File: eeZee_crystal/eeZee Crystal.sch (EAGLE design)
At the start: 4 parts, among them Q1 16MHz

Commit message: Changed 3-pin header to vertical style (displays better in Eagle)
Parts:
- JP1: device pinhead-2:PINHD-1X03_2.54-90°-S -> pinhead-2:PINHD-1X03_2.54-S
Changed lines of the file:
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@@
 <?xml version="1.0" encoding="utf-8"?>
 <!DOCTYPE eagle SYSTEM "eagle.dtd">
-<eagle version="6.0">
+<eagle version="6.1">
 <drawing>
 <settings>
@@
 <layer number="49" name="Reference" color="7" fill="1" visible="yes" active="no"/>
 <layer number="50" name="dxf" color="7" fill="1" visible="yes" active="no"/>
-<layer number="51" name="tDocu" color="7" fill="1" visible="yes" active="no"/>
+<layer number="51" name="tDocu" color="11" fill="1" visible="yes" active="no"/>
 <layer number="52" name="bDocu" color="7" fill="1" visible="yes" active="no"/>
 <layer number="53" name="tPadExt" color="7" fill="1" visible="yes" active="no"/>
@@
 <attribute name="PARTNO" value="C1608C0G1H080D"/>
 </part>
-<part name="JP1" library="pinhead-2" deviceset="PINHD-1X03" device="_2.54-90°-S" value="XTAL">
+<part name="JP1" library="pinhead-2" deviceset="PINHD-1X03" device="_2.54-S" value="XTAL">
 <attribute name="BOM" value="EXCLUDE"/>
 </part>

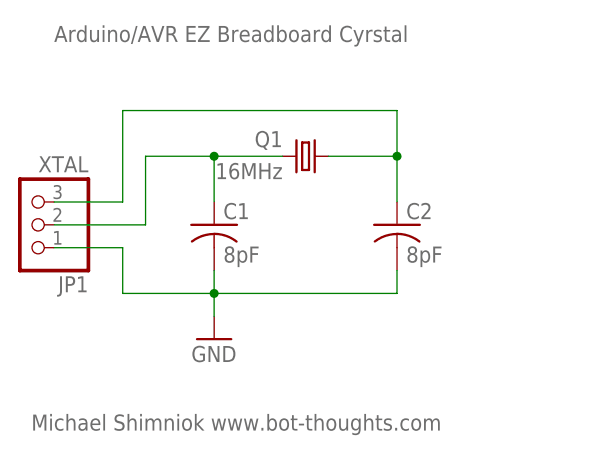
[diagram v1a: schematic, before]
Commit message: Resized board narrower and aligned to inches. Added silk for multiple frequencies. Mitred corners. Changed silk print sizes.
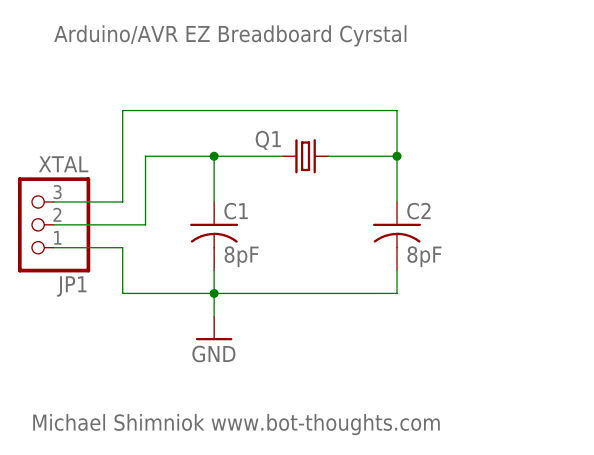
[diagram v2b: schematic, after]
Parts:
- Q1: value 16MHz -> (none)
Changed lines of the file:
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@@
 <?xml version="1.0" encoding="utf-8"?>
 <!DOCTYPE eagle SYSTEM "eagle.dtd">
-<eagle version="6.1">
+<eagle version="6.4">
 <drawing>
 <settings>
@@
 <grid distance="0.1" unitdist="inch" unit="inch" style="lines" multiple="1" display="no" altdistance="0.01" altunitdist="inch" altunit="inch"/>
 <layers>
-<layer number="1" name="Top" color="4" fill="1" visible="yes" active="no"/>
-<layer number="16" name="Bottom" color="1" fill="1" visible="yes" active="no"/>
-<layer number="17" name="Pads" color="2" fill="1" visible="yes" active="no"/>
-<layer number="18" name="Vias" color="2" fill="1" visible="yes" active="no"/>
-<layer number="19" name="Unrouted" color="6" fill="1" visible="yes" active="no"/>
-<layer number="20" name="Dimension" color="15" fill="1" visible="yes" active="no"/>
-<layer number="21" name="tPlace" color="7" fill="1" visible="yes" active="no"/>
-<layer number="22" name="bPlace" color="7" fill="1" visible="yes" active="no"/>
-<layer number="23" name="tOrigins" color="15" fill="1" visible="yes" active="no"/>
-<layer number="24" name="bOrigins" color="15" fill="1" visible="yes" active="no"/>
-<layer number="25" name="tNames" color="7" fill="1" visible="yes" active="no"/>
-<layer number="26" name="bNames" color="7" fill="1" visible="yes" active="no"/>
-<layer number="27" name="tValues" color="7" fill="1" visible="yes" active="no"/>
-<layer number="28" name="bValues" color="7" fill="1" visible="yes" active="no"/>
+<layer number="1" name="Top" color="4" fill="1" visible="no" active="no"/>
+<layer number="16" name="Bottom" color="1" fill="1" visible="no" active="no"/>
+<layer number="17" name="Pads" color="2" fill="1" visible="no" active="no"/>
+<layer number="18" name="Vias" color="2" fill="1" visible="no" active="no"/>
+<layer number="19" name="Unrouted" color="6" fill="1" visible="no" active="no"/>
+<layer number="20" name="Dimension" color="15" fill="1" visible="no" active="no"/>
+<layer number="21" name="tPlace" color="7" fill="1" visible="no" active="no"/>
+<layer number="22" name="bPlace" color="7" fill="1" visible="no" active="no"/>
+<layer number="23" name="tOrigins" color="15" fill="1" visible="no" active="no"/>
+<layer number="24" name="bOrigins" color="15" fill="1" visible="no" active="no"/>
+<layer number="25" name="tNames" color="7" fill="1" visible="no" active="no"/>
+<layer number="26" name="bNames" color="7" fill="1" visible="no" active="no"/>
+<layer number="27" name="tValues" color="7" fill="1" visible="no" active="no"/>
+<layer number="28" name="bValues" color="7" fill="1" visible="no" active="no"/>
 <layer number="29" name="tStop" color="7" fill="3" visible="no" active="no"/>
 <layer number="30" name="bStop" color="7" fill="6" visible="no" active="no"/>
@@
 <layer number="35" name="tGlue" color="7" fill="4" visible="no" active="no"/>
 <layer number="36" name="bGlue" color="7" fill="5" visible="no" active="no"/>
-<layer number="37" name="tTest" color="7" fill="1" visible="yes" active="no"/>
-<layer number="38" name="bTest" color="7" fill="1" visible="yes" active="no"/>
+<layer number="37" name="tTest" color="7" fill="1" visible="no" active="no"/>
+<layer number="38" name="bTest" color="7" fill="1" visible="no" active="no"/>
 <layer number="39" name="tKeepout" color="4" fill="11" visible="no" active="no"/>
 <layer number="40" name="bKeepout" color="1" fill="11" visible="no" active="no"/>
@@
 <layer number="44" name="Drills" color="7" fill="1" visible="no" active="no"/>
 <layer number="45" name="Holes" color="7" fill="1" visible="no" active="no"/>
-<layer number="46" name="Milling" color="3" fill="1" visible="yes" active="no"/>
-<layer number="47" name="Measures" color="7" fill="1" visible="yes" active="no"/>
-<layer number="48" name="Document" color="7" fill="1" visible="yes" active="no"/>
-<layer number="49" name="Reference" color="7" fill="1" visible="yes" active="no"/>
-<layer number="50" name="dxf" color="7" fill="1" visible="yes" active="no"/>
-<layer number="51" name="tDocu" color="11" fill="1" visible="yes" active="no"/>
-<layer number="52" name="bDocu" color="7" fill="1" visible="yes" active="no"/>
-<layer number="53" name="tPadExt" color="7" fill="1" visible="yes" active="no"/>
-<layer number="54" name="bPadExt" color="1" fill="1" visible="yes" active="no"/>
-<layer number="56" name="wert" color="7" fill="1" visible="yes" active="no"/>
+<layer number="46" name="Milling" color="3" fill="1" visible="no" active="no"/>
+<layer number="47" name="Measures" color="7" fill="1" visible="no" active="no"/>
+<layer number="48" name="Document" color="7" fill="1" visible="no" active="no"/>
+<layer number="49" name="Reference" color="7" fill="1" visible="no" active="no"/>
+<layer number="50" name="dxf" color="7" fill="1" visible="no" active="no"/>
+<layer number="51" name="tDocu" color="11" fill="1" visible="no" active="no"/>
+<layer number="52" name="bDocu" color="7" fill="1" visible="no" active="no"/>
+<layer number="53" name="tPadExt" color="7" fill="1" visible="no" active="no"/>
+<layer number="54" name="bPadExt" color="1" fill="1" visible="no" active="no"/>
+<layer number="56" name="wert" color="7" fill="1" visible="no" active="no"/>
 <layer number="91" name="Nets" color="2" fill="1" visible="yes" active="yes"/>
 <layer number="92" name="Busses" color="1" fill="1" visible="yes" active="yes"/>
@@
 </classes>
 <parts>
-<part name="Q1" library="mes_crystal" deviceset="CRYSTAL" device="NDK5X3" value="16MHz">
+<part name="Q1" library="mes_crystal" deviceset="CRYSTAL" device="NDK5X3">
 <attribute name="PARTNO" value="NX5032GA-16.000000MHZ-LN-CD-1"/>
 </part>

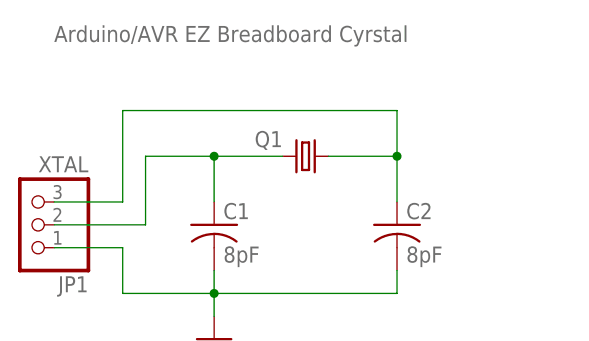
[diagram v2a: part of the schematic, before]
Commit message: Increaed spacing to 8/10mil for most objects, reduced distance to 10mil.
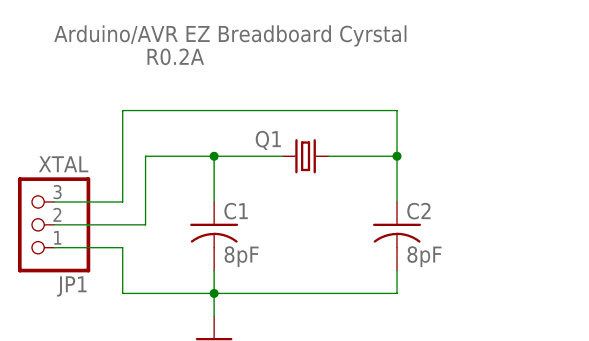
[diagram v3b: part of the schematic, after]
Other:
- note added: "R0.2A"
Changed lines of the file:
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@@
 <text x="25.4" y="48.26" size="1.778" layer="95">Arduino/AVR EZ Breadboard Cyrstal</text>
 <text x="22.86" y="5.08" size="1.778" layer="95">Michael Shimniok www.bot-thoughts.com</text>
+<text x="35.56" y="45.72" size="1.778" layer="95">R0.2A</text>
 </plain>
 <instances>

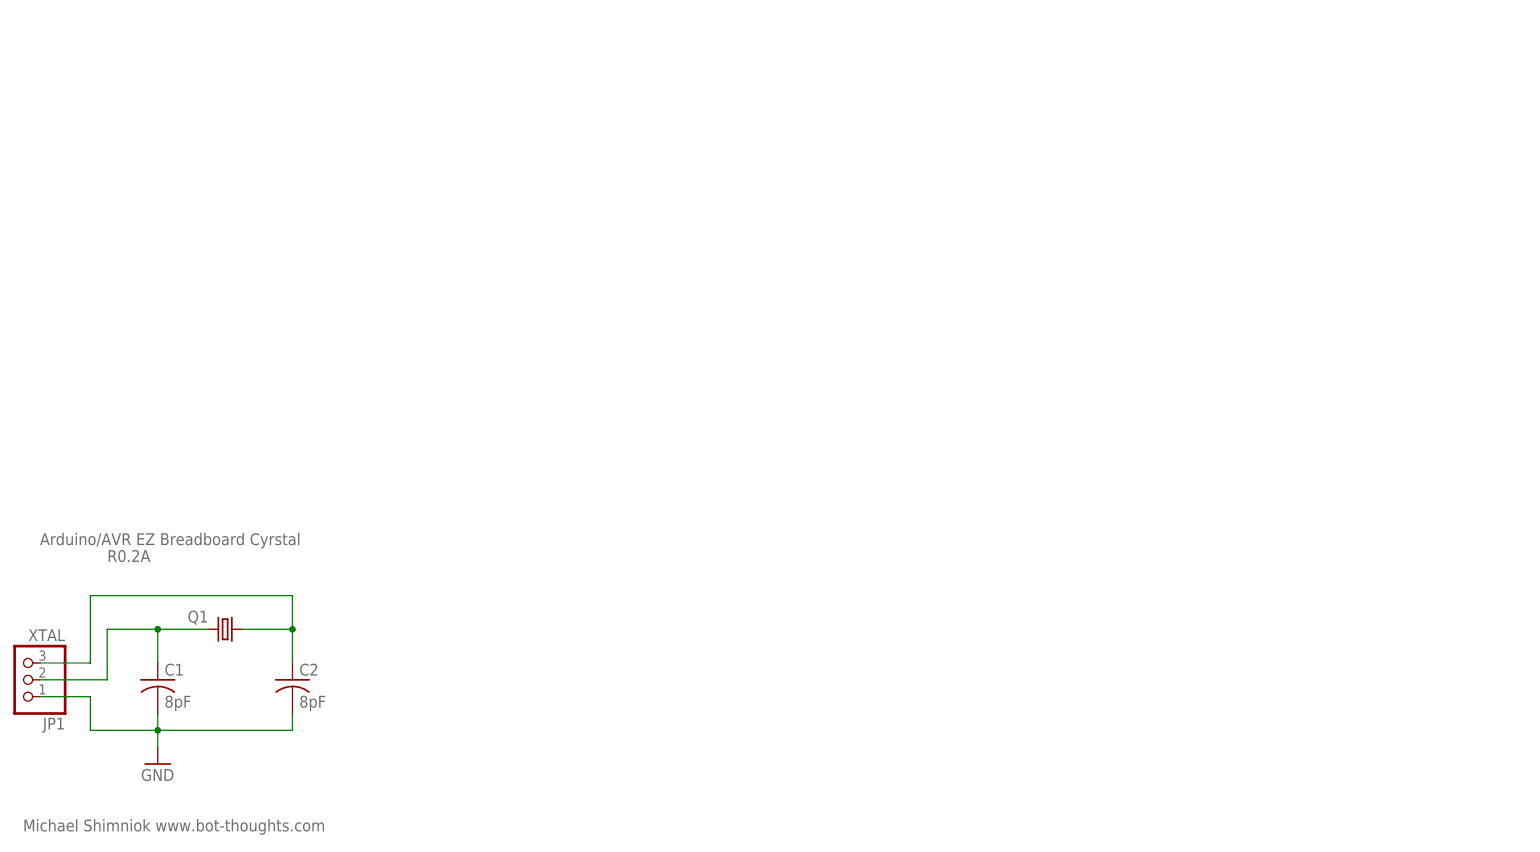
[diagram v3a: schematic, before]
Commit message: Modified schematic for easier reading, added letter box. Added 20MHz option to board.
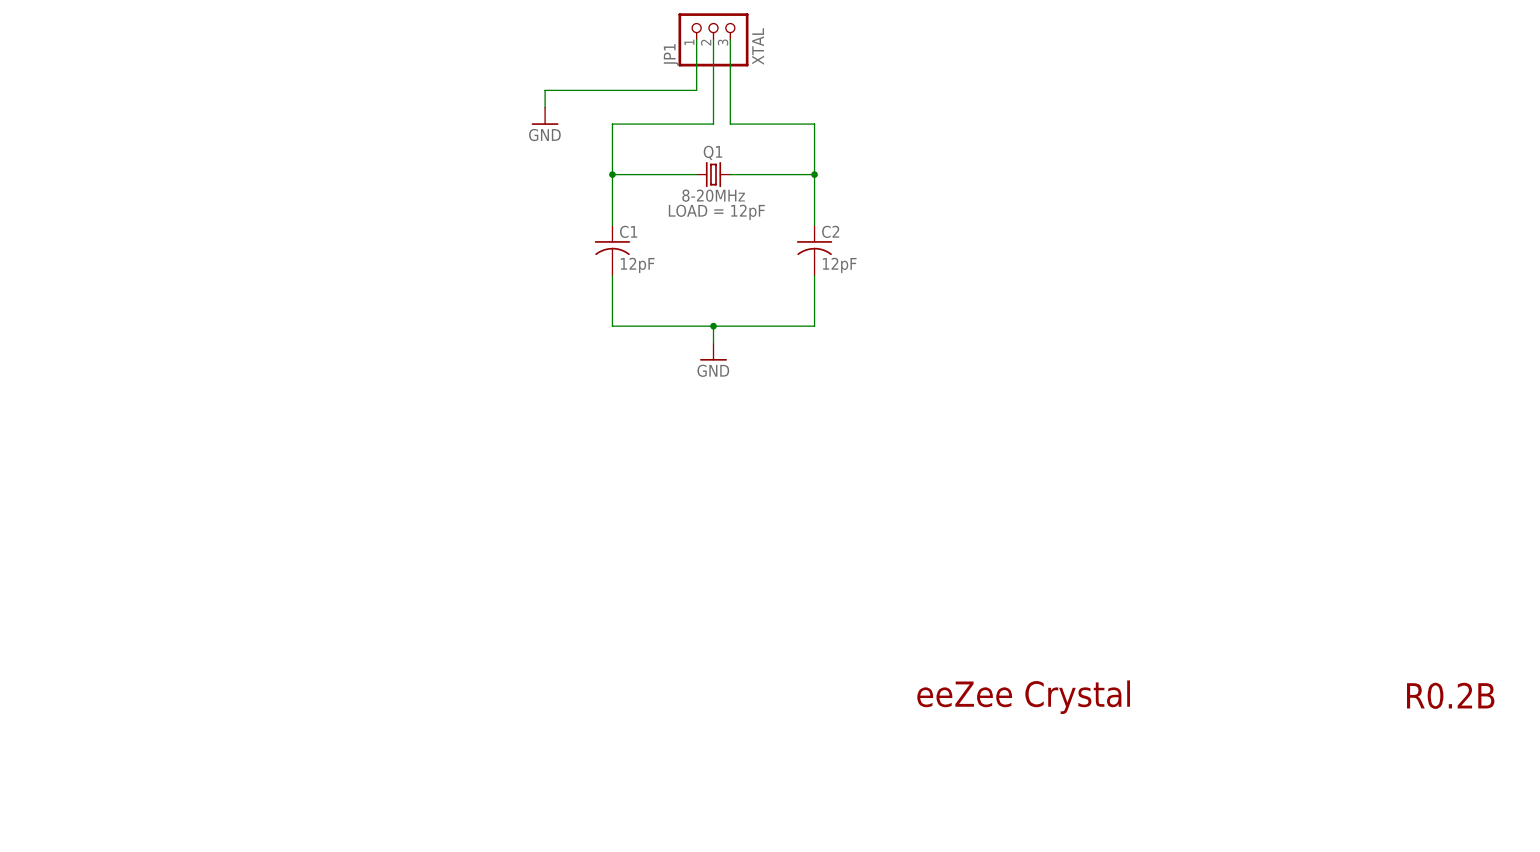
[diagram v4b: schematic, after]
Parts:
- C1, C2: value 8pF -> 12pF
- Q1: value (none) -> 8-20MHz; LOAD (none) -> 12pF
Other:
- note added: "R0.2B"
- note added: "eeZee Crystal"
- note removed: "Arduino/AVR EZ Breadboard Cyrstal"
- note removed: "Michael Shimniok www.bot-thoughts.com"
- note removed: "R0.2A"
- moved on the sheet: C1, C2, JP1, Q1
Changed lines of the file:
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@@
 </classes>
 <parts>
-<part name="Q1" library="mes_crystal" deviceset="CRYSTAL" device="NDK5X3">
+<part name="Q1" library="mes_crystal" deviceset="CRYSTAL" device="NDK5X3" value="8-20MHz">
+<attribute name="LOAD" value="12pF"/>
 <attribute name="PARTNO" value="NX5032GA-16.000000MHZ-LN-CD-1"/>
 </part>
-<part name="C1" library="rcl" deviceset="C-US" device="C0603" value="8pF">
+<part name="C1" library="rcl" deviceset="C-US" device="C0603" value="12pF">
 <attribute name="BOM" value="INCLUDE"/>
 <attribute name="PARTNO" value="C1608C0G1H080D"/>
 </part>
-<part name="C2" library="rcl" deviceset="C-US" device="C0603" value="8pF">
+<part name="C2" library="rcl" deviceset="C-US" device="C0603" value="12pF">
 <attribute name="BOM" value="INCLUDE"/>
 <attribute name="PARTNO" value="C1608C0G1H080D"/>
@@
 </part>
 <part name="GND1" library="mes" deviceset="GND" device=""/>
+<part name="FRAME1" library="bt" deviceset="LETTER_L" device=""/>
+<part name="GND2" library="mes" deviceset="GND" device=""/>
 </parts>
 <sheets>
 <sheet>
 <plain>
-<text x="25.4" y="48.26" size="1.778" layer="95">Arduino/AVR EZ Breadboard Cyrstal</text>
-<text x="22.86" y="5.08" size="1.778" layer="95">Michael Shimniok www.bot-thoughts.com</text>
-<text x="35.56" y="45.72" size="1.778" layer="95">R0.2A</text>
+<text x="157.48" y="23.876" size="3.81" layer="94">eeZee Crystal</text>
+<text x="231.14" y="23.622" size="3.81" layer="94">R0.2B</text>
 </plain>
 <instances>
-<instance part="Q1" gate="G$1" x="53.34" y="35.56" rot="MR0">
-<attribute name="PARTNO" x="53.34" y="35.56" size="1.778" layer="96" display="off"/>
+<instance part="Q1" gate="G$1" x="127" y="104.14" smashed="yes" rot="MR0">
+<attribute name="PARTNO" x="127" y="104.14" size="1.778" layer="96" display="off"/>
+<attribute name="LOAD" x="134.874" y="97.79" size="1.778" layer="96" rot="MR0" display="both"/>
+<attribute name="NAME" x="128.524" y="106.68" size="1.778" layer="95" rot="MR0"/>
+<attribute name="VALUE" x="131.826" y="100.076" size="1.778" layer="96" rot="MR0"/>
 </instance>
-<instance part="C1" gate="G$1" x="43.18" y="27.94">
-<attribute name="PARTNO" value="C1608C0G1H080D" x="43.18" y="27.94" size="1.778" layer="96" display="off"/>
-<attribute name="BOM" value="INCLUDE" x="43.18" y="27.94" size="1.778" layer="96" display="off"/>
+<instance part="C1" gate="G$1" x="111.76" y="93.98">
+<attribute name="PARTNO" value="C1608C0G1H080D" x="111.76" y="93.98" size="1.778" layer="96" display="off"/>
+<attribute name="BOM" value="INCLUDE" x="111.76" y="93.98" size="1.778" layer="96" display="off"/>
 </instance>
-<instance part="C2" gate="G$1" x="63.5" y="27.94">
-<attribute name="PARTNO" value="C1608C0G1H080D" x="63.5" y="27.94" size="1.778" layer="96" display="off"/>
-<attribute name="BOM" value="INCLUDE" x="63.5" y="27.94" size="1.778" layer="96" display="off"/>
+<instance part="C2" gate="G$1" x="142.24" y="93.98">
+<attribute name="PARTNO" value="C1608C0G1H080D" x="142.24" y="93.98" size="1.778" layer="96" display="off"/>
+<attribute name="BOM" value="INCLUDE" x="142.24" y="93.98" size="1.778" layer="96" display="off"/>
 </instance>
-<instance part="JP1" gate="A" x="22.86" y="27.94" rot="R180">
-<attribute name="BOM" value="EXCLUDE" x="22.86" y="27.94" size="1.778" layer="96" display="off"/>
+<instance part="JP1" gate="A" x="127" y="127" rot="R90">
+<attribute name="BOM" value="EXCLUDE" x="127" y="127" size="1.778" layer="96" rot="R270" display="off"/>
 </instance>
-<instance part="GND1" gate="1" x="43.18" y="15.24"/>
+<instance part="GND1" gate="1" x="127" y="76.2"/>
+<instance part="FRAME1" gate="G$1" x="0" y="0"/>
+<instance part="FRAME1" gate="G$2" x="147.32" y="2.54"/>
+<instance part="GND2" gate="1" x="101.6" y="111.76"/>
 </instances>
 <busses>
@@
 <segment>
 <pinref part="JP1" gate="A" pin="1"/>
-<wire x1="25.4" y1="25.4" x2="33.02" y2="25.4" width="0.1524" layer="91"/>
-<wire x1="33.02" y1="25.4" x2="33.02" y2="20.32" width="0.1524" layer="91"/>
-<wire x1="33.02" y1="20.32" x2="43.18" y2="20.32" width="0.1524" layer="91"/>
+<wire x1="124.46" y1="124.46" x2="124.46" y2="116.84" width="0.1524" layer="91"/>
+<wire x1="124.46" y1="116.84" x2="101.6" y2="116.84" width="0.1524" layer="91"/>
+<wire x1="101.6" y1="116.84" x2="101.6" y2="114.3" width="0.1524" layer="91"/>
+<pinref part="GND2" gate="1" pin="GND"/>
+</segment>
+<segment>
 <pinref part="C2" gate="G$1" pin="2"/>
-<wire x1="43.18" y1="20.32" x2="63.5" y2="20.32" width="0.1524" layer="91"/>
-<wire x1="63.5" y1="20.32" x2="63.5" y2="22.86" width="0.1524" layer="91"/>
+<wire x1="127" y1="81.28" x2="142.24" y2="81.28" width="0.1524" layer="91"/>
+<wire x1="142.24" y1="81.28" x2="142.24" y2="88.9" width="0.1524" layer="91"/>
 <pinref part="C1" gate="G$1" pin="2"/>
-<wire x1="43.18" y1="20.32" x2="43.18" y2="22.86" width="0.1524" layer="91"/>
-<junction x="43.18" y="20.32"/>
+<wire x1="127" y1="81.28" x2="111.76" y2="81.28" width="0.1524" layer="91"/>
+<wire x1="111.76" y1="81.28" x2="111.76" y2="88.9" width="0.1524" layer="91"/>
+<junction x="127" y="81.28"/>
 <pinref part="GND1" gate="1" pin="GND"/>
-<wire x1="43.18" y1="17.78" x2="43.18" y2="20.32" width="0.1524" layer="91"/>
+<wire x1="127" y1="78.74" x2="127" y2="81.28" width="0.1524" layer="91"/>
 </segment>
 </net>
@@
 <segment>
 <pinref part="C1" gate="G$1" pin="1"/>
-<wire x1="43.18" y1="35.56" x2="43.18" y2="30.48" width="0.1524" layer="91"/>
+<wire x1="111.76" y1="104.14" x2="111.76" y2="96.52" width="0.1524" layer="91"/>
 <pinref part="JP1" gate="A" pin="2"/>
-<wire x1="25.4" y1="27.94" x2="35.56" y2="27.94" width="0.1524" layer="91"/>
-<wire x1="35.56" y1="27.94" x2="35.56" y2="35.56" width="0.1524" layer="91"/>
-<wire x1="35.56" y1="35.56" x2="43.18" y2="35.56" width="0.1524" layer="91"/>
+<wire x1="127" y1="124.46" x2="127" y2="111.76" width="0.1524" layer="91"/>
+<wire x1="127" y1="111.76" x2="111.76" y2="111.76" width="0.1524" layer="91"/>
+<wire x1="111.76" y1="111.76" x2="111.76" y2="104.14" width="0.1524" layer="91"/>
 <pinref part="Q1" gate="G$1" pin="2"/>
-<wire x1="43.18" y1="35.56" x2="50.8" y2="35.56" width="0.1524" layer="91"/>
-<junction x="43.18" y="35.56"/>
+<wire x1="111.76" y1="104.14" x2="124.46" y2="104.14" width="0.1524" layer="91"/>
+<junction x="111.76" y="104.14"/>
 </segment>
 </net>
@@
 <pinref part="C2" gate="G$1" pin="1"/>
 <pinref part="JP1" gate="A" pin="3"/>
-<wire x1="25.4" y1="30.48" x2="33.02" y2="30.48" width="0.1524" layer="91"/>
-<wire x1="33.02" y1="30.48" x2="33.02" y2="40.64" width="0.1524" layer="91"/>
-<wire x1="33.02" y1="40.64" x2="63.5" y2="40.64" width="0.1524" layer="91"/>
-<wire x1="63.5" y1="40.64" x2="63.5" y2="35.56" width="0.1524" layer="91"/>
+<wire x1="129.54" y1="124.46" x2="129.54" y2="111.76" width="0.1524" layer="91"/>
+<wire x1="129.54" y1="111.76" x2="142.24" y2="111.76" width="0.1524" layer="91"/>
+<wire x1="142.24" y1="111.76" x2="142.24" y2="104.14" width="0.1524" layer="91"/>
 <pinref part="Q1" gate="G$1" pin="1"/>
-<wire x1="63.5" y1="35.56" x2="63.5" y2="30.48" width="0.1524" layer="91"/>
-<wire x1="55.88" y1="35.56" x2="63.5" y2="35.56" width="0.1524" layer="91"/>
-<junction x="63.5" y="35.56"/>
+<wire x1="142.24" y1="104.14" x2="142.24" y2="96.52" width="0.1524" layer="91"/>
+<wire x1="129.54" y1="104.14" x2="142.24" y2="104.14" width="0.1524" layer="91"/>
+<junction x="142.24" y="104.14"/>
 </segment>
 </net>
